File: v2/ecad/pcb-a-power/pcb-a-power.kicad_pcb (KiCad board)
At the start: 4 copper layers, 285 x 160 mm, 214 parts, among them Q5 2N7002: Pi GPIO high = pull K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, U19 PCA9555PW (0x21), U20 BQ25792 1S charger from SHORE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, U21 BQ34Z100-G1 gauge (I2C 0x55, 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, U22 TPS61288L boost +5V_M1 (15 A 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, U23 TPS61288L boost +5V_M2 (15 A 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, U24 TPS61288L boost +5V_PI (15 A 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, U25 LTC2954CTS8-1 push-button on/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, U26 TPS259571DSGR eFuse 12 V 2.0 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, U28 TPS2065CDBV, U29 INA219AIDCN, U30 USBLC6-2SC6, U31 PCA9555PW (0x24): wall port, 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, U5 TPS563201 3.3 V buck from M1

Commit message: fix(release): A20 and E4 relabelled GNSS post-route, E5 block with one outline around the power targets; deliverables, order and review sets rebuilt [MESHSAT-795]
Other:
- board text added: "BM GNSS"
- board text added: "SMA GNSS"
- board text removed: "BM WIFI 5.8"
- board text removed: "SMA WIFI 5.8"
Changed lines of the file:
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@@
 		)
 	)
-	(gr_text "SMA WIFI 5.8"
+	(gr_text "SMA GNSS"
 		(at 124 160 0)
 		(layer "F.SilkS")
@@
 		)
 	)
-	(gr_text "BM WIFI 5.8"
+	(gr_text "BM GNSS"
 		(at 124 184 0)
 		(layer "B.SilkS")

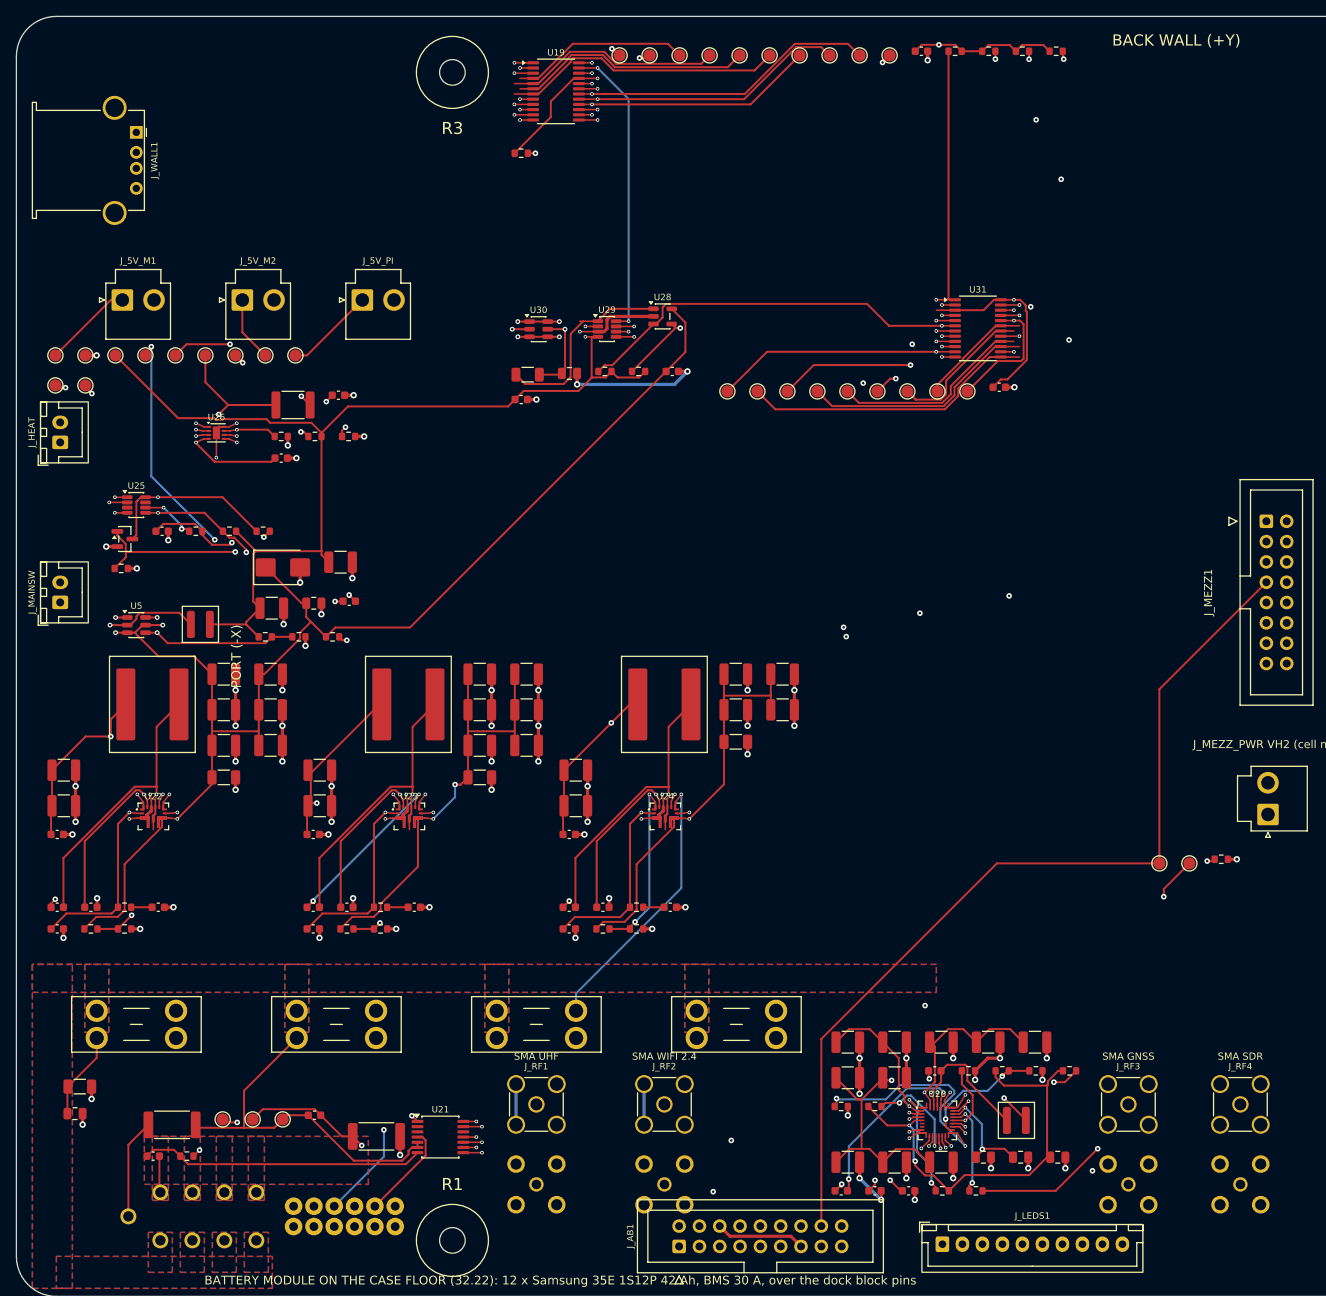
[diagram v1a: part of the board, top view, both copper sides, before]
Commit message: feat(pcb-a): A21, PCB-A re-routed with the net classes applied: rail islands and bottom bands, boost feeds on In2 and B.Cu, 0.6 mm cell-node links, USB pairs 0.2/0.15 [MESHSAT-795]
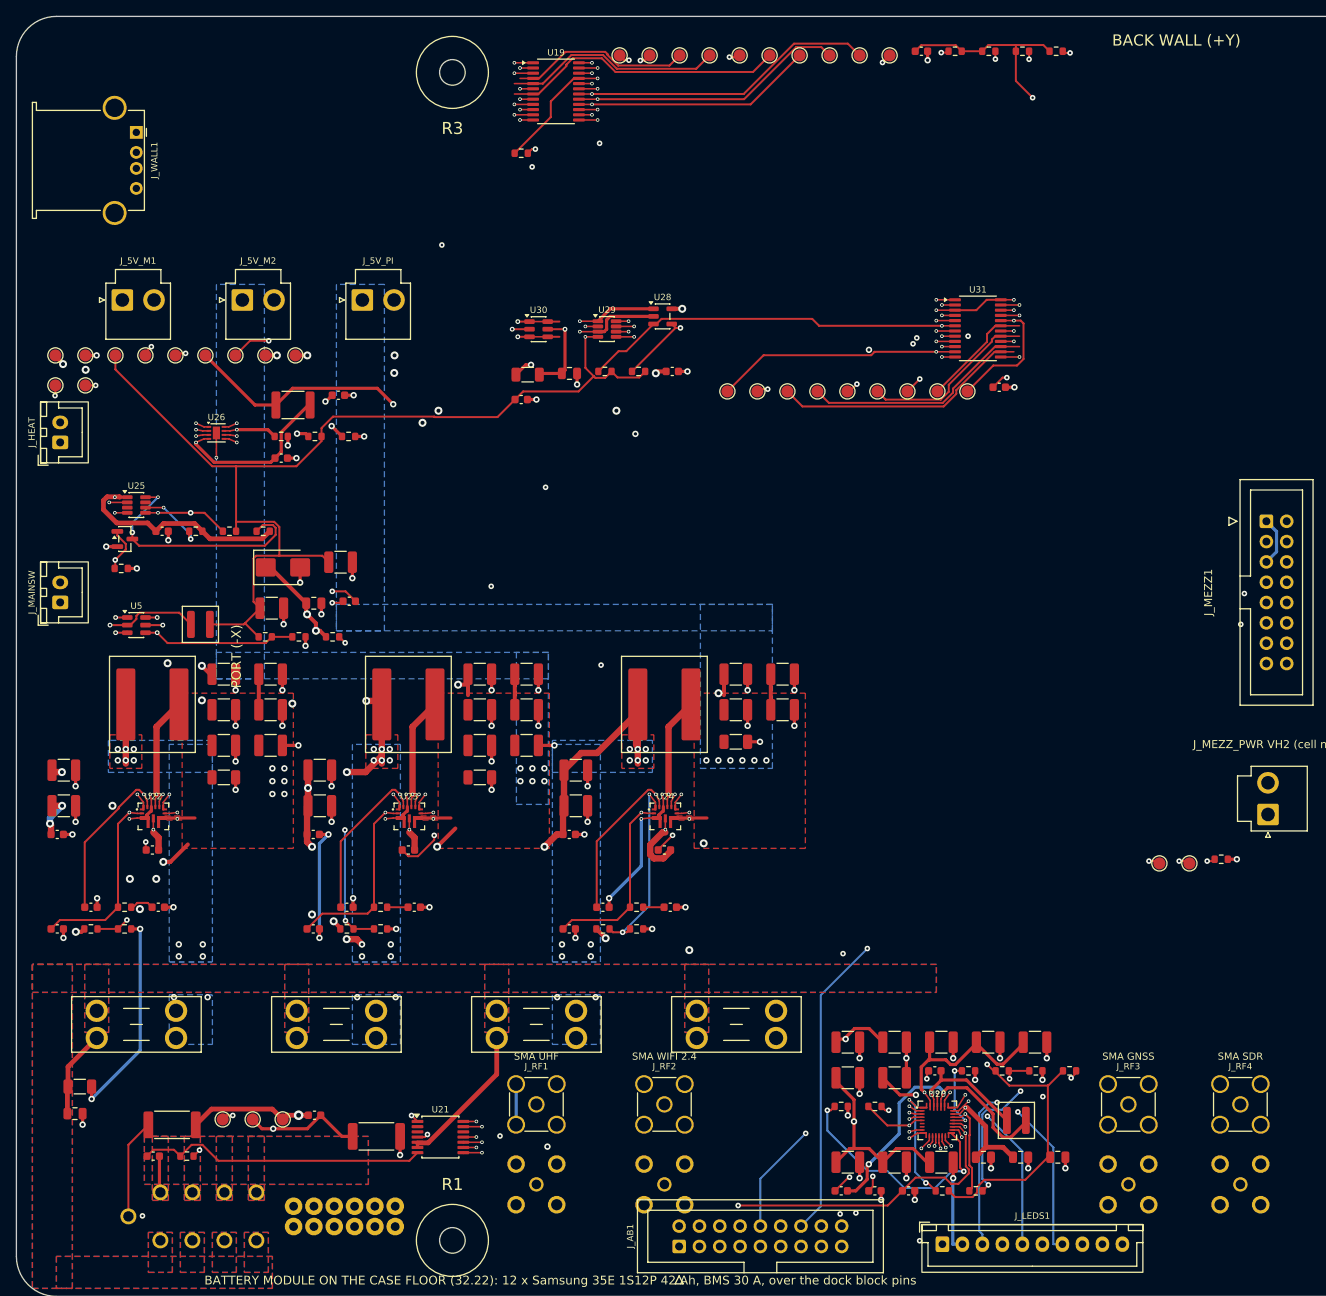
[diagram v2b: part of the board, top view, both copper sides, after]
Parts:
- moved C84 13.9 mm to (66.0, 134.2)
- moved C38 13.9 mm to (2.00, 134.2)
- moved C71 13.9 mm to (34.0, 134.2)
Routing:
- net GND: track 1441.6 -> 1514.2 mm
- net /+5V_M2: track 136.1 -> 103.6 mm, vias 2 -> 12
- net /SHORE_12V: track 241.7 -> 272.8 mm, vias 5 -> 8
- net /SCL: track 338.2 -> 308.0 mm, vias 7 -> 6
- net /BOOST1_IN: track 65.1 -> 84.0 mm, vias 2 -> 19
- net /I2S_BCLK: track 131.5 -> 150.2 mm, vias 1 -> 0
- net /LED_MESH_K: track 198.1 -> 180.6 mm
- net /BST3: track 26.9 -> 9.50 mm
- net /LED_LTE_K: track 198.9 -> 181.9 mm, vias 2 -> 1
- net /DOCK_SPARE: track 130.7 -> 147.7 mm, vias 1 -> 2
- net /LED_SYS_K: track 208.3 -> 191.5 mm, vias 2 -> 1
- net /+5V_PI: track 149.7 -> 133.0 mm, vias 1 -> 15
- net /PI_KILL: track 131.4 -> 147.1 mm, vias 1 -> 2
- net /SW1: track 38.4 -> 22.8 mm, vias 1 -> 2
- net /SW2: track 38.4 -> 22.8 mm, vias 1 -> 2
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- added copper zone on F.Cu, net /+5V_M1
- added copper zone on B.Cu, net /+5V_M2
- added copper zone on F.Cu, net /+5V_M2
- added copper zone on B.Cu, net /+5V_PI
- added copper zone on F.Cu, net /+5V_PI
- added copper zone on B.Cu, net /BOOST1_IN
- added copper zone on F.Cu, net /BOOST1_IN
- added copper zone on In1.Cu, net /BOOST1_IN
- added copper zone on In2.Cu, net /BOOST1_IN
- added copper zone on B.Cu, net /BOOST2_IN
- added copper zone on F.Cu, net /BOOST2_IN
- added copper zone on In1.Cu, net /BOOST2_IN
- added copper zone on In2.Cu, net /BOOST2_IN
- added copper zone on B.Cu, net /BOOST3_IN
- added copper zone on F.Cu, net /BOOST3_IN
- added copper zone on In1.Cu, net /BOOST3_IN
- added copper zone on In2.Cu, net /BOOST3_IN

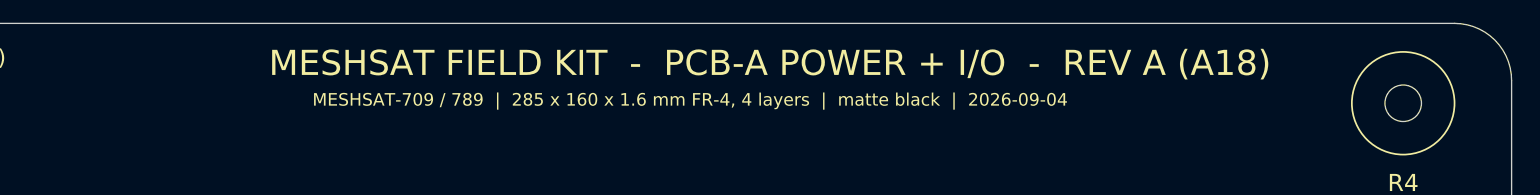
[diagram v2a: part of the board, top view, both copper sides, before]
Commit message: fix(pcb): A21 and D7 boards retitled to their phase and date, deliverables re-exported [MESHSAT-795]
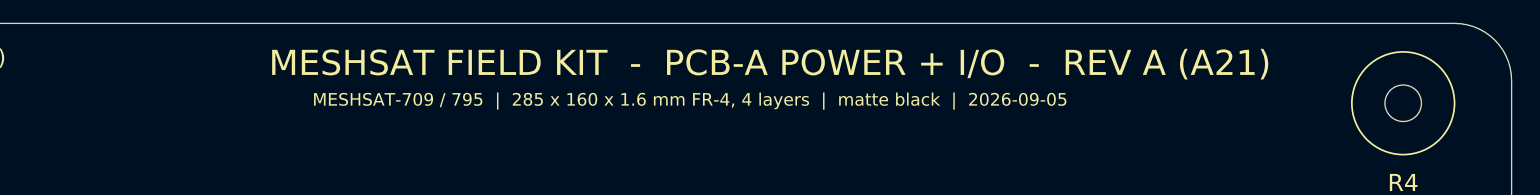
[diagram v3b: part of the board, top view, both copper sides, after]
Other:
- board text added: "MESHSAT FIELD KIT - PCB-A POWER + I/O - REV A (A21)"
- board text added: "MESHSAT-709 / 795 | 285 x 160 x 1.6 mm FR-4, 4 layers | matte black | 2026-09-05"
- board text removed: "MESHSAT FIELD KIT - PCB-A POWER + I/O - REV A (A18)"
- board text removed: "MESHSAT-709 / 789 | 285 x 160 x 1.6 mm FR-4, 4 layers | matte black | 2026-09-04"
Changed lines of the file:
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@@
 	(title_block
 		(title "MeshSat Field Kit carrier - PCB-B COMPUTE")
-		(date "2026-09-02")
-		(rev "A")
+		(date "2026-09-05")
+		(rev "A (A21)")
 		(company "MeshSat")
 		(comment 1 "MESHSAT-709. Case-centred frame. Phase B1 mechanical + placement. tools/gen_pcb_b.py")
@@
 		)
 	)
-	(gr_text "MESHSAT-709 / 789  |  285 x 160 x 1.6 mm FR-4, 4 layers  |  matte black  |  2026-09-04"
+	(gr_text "MESHSAT-709 / 795  |  285 x 160 x 1.6 mm FR-4, 4 layers  |  matte black  |  2026-09-05"
 		(at 198 36.7 0)
 		(layer "F.SilkS")
@@
 		)
 	)
-	(gr_text "MESHSAT FIELD KIT  -  PCB-A POWER + I/O  -  REV A (A18)"
+	(gr_text "MESHSAT FIELD KIT  -  PCB-A POWER + I/O  -  REV A (A21)"
 		(at 205 33.5 0)
 		(layer "F.SilkS")

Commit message: feat(release): A22 (six layers, run 12 with the hand closures) routed clean on the box, deliverable meshsat-pcb-a-revA-A22 [MESHSAT-830]
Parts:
- removed C105: 100n, C_0603_1608Metric
- removed F2: 10 A mini blade (Keystone 3568 holder): pack node to the 8 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, Fuseholder_Blade_Mini_Keystone_3568
- removed F3: 10 A mini blade (Keystone 3568 holder): pack node to the M1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, Fuseholder_Blade_Mini_Keystone_3568
- removed F4: 10 A mini blade (Keystone 3568 holder): pack node to the M2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, Fuseholder_Blade_Mini_Keystone_3568
- removed F5: 15 A mini blade (Keystone 3568 holder): pack node to the Pi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, Fuseholder_Blade_Mini_Keystone_3568
- removed F6: 2.5A hold 30V 1812, Fuse_1812_4532Metric
- removed J_5V_M1: rail M1 to PCB-B J_5V_M1 (JST-VH, 18 AWG): + -, JST_VH_B2P-VH_1x02_P3.96mm_Vertical
- removed J_5V_M2: rail M2 to PCB-B J_5V_M2 (JST-VH, 18 AWG): + -, JST_VH_B2P-VH_1x02_P3.96mm_Vertical
- removed J_5V_PI: Pi rail 5.1 V 5 A to PCB-B J_5V_PI (JST-VH, 18 AWG): + -, JST_VH_B2P-VH_1x02_P3.96mm_Vertical
- removed J_LEDS1: front-wall LED row (XH2.5): PWR MESH SAT LTE SYS, JST_XH_B10B-XH-A_1x10_P2.50mm_Vertical
- removed J_WALL1: USB-A receptacle, internal cable to the Glenair 233-370 wal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, USB_A_Stewart_SS-52100-001_Horizontal
- removed RT1: 10k NTC 0603 1% (gauge temperature, beside the dock pins; t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, R_0603_1608Metric
- removed TP1: +5V_M1, TestPoint_Pad_D1.5mm
- removed TP2: GND, TestPoint_Pad_D1.5mm
- removed TP27: EXP2_SP8, TestPoint_Pad_D1.5mm
- removed TP29: EXP_SP4, TestPoint_Pad_D1.5mm
- removed TP30: EXP_SP5, TestPoint_Pad_D1.5mm
- removed TP31: EXP_SP6, TestPoint_Pad_D1.5mm
- removed TP32: EXP_SP7, TestPoint_Pad_D1.5mm
- removed TP33: EXP_SP8, TestPoint_Pad_D1.5mm
- removed TP34: EXP_SP9, TestPoint_Pad_D1.5mm
- removed TP35: EXP_SP10, TestPoint_Pad_D1.5mm
- removed TP36: EXP_SP11, TestPoint_Pad_D1.5mm
- removed U20: BQ25792 1S charger from SHORE_12V (3 A set over ILIM_HIZ, 7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, Texas_RQM0029A_QFN-29_4x4mm
- removed U24: TPS61288L boost +5V_PI (15 A switch, 500 kHz, no MODE pin), Texas_RQQ0011A_VQFN-HR-11_2.5x3mm
- removed U25: LTC2954CTS8-1 push-button on/off controller, TSOT-23-8
- removed U30: USBLC6-2SC6, SOT-23-6
- removed U31: PCA9555PW (0x24): wall port, heating pad, charger, gauge, TSSOP-24_4.4x7.8mm_P0.65mm
- added C1: 100u 25V, C_1206_3216Metric, F.Cu at (40.8, 166.6)
- added C10: 100n 25V, C_0603_1608Metric, F.Cu at (38.3, 75.6)
- added C102: 10n, C_0603_1608Metric, F.Cu at (236.1, 60.2)
- added C103: 100n, C_0603_1608Metric, F.Cu at (244.5, 62.9)
- added C109: 22u 50V X7R 1210, C_1210_3225Metric, F.Cu at (136.9, 139.7)
- added C11: 22u 50V X7R 1210, C_1210_3225Metric, F.Cu at (78.9, 66.2)
- added C110: 22u 50V X7R 1210, C_1210_3225Metric, F.Cu at (142.8, 139.7)
- added C111: 22u 50V X7R 1210, C_1210_3225Metric, F.Cu at (136.9, 144.1)
- added C112: 3.3n, C_0603_1608Metric, F.Cu at (90.3, 73.0)
- added C113: 3.3n, C_0603_1608Metric, F.Cu at (106.3, 73.0)
- added C114: 3.3n, C_0603_1608Metric, F.Cu at (122.3, 73.0)
- added C115: 3.3n, C_0603_1608Metric, F.Cu at (142.5, 73.0)
- added C116: 22u 50V X7R 1210, C_1210_3225Metric, F.Cu at (188.8, 61.0)
- added C117: 22u 50V X7R 1210, C_1210_3225Metric, F.Cu at (194.6, 61.0)
- added C118: 22u 50V X7R 1210, C_1210_3225Metric, F.Cu at (200.5, 61.0)
- added C119: 22u 50V X7R 1210, C_1210_3225Metric, F.Cu at (206.3, 61.0)
- added C12: 22u 50V X7R 1210, C_1210_3225Metric, F.Cu at (34.9, 72.0)
- added C120: 10u 25V 1210, C_1210_3225Metric, F.Cu at (161.8, 57.0)
- added C16: 100n 25V, C_0603_1608Metric, F.Cu at (58.1, 105.4)
- added C17: 100n 25V, C_0603_1608Metric, F.Cu at (62.3, 105.4)
- added C18: 3.3u, C_0805_2012Metric, F.Cu at (42.4, 105.6)
- added C19: 1u, C_0603_1608Metric, F.Cu at (70.7, 105.4)
- added C2: 100u 25V, C_1206_3216Metric, F.Cu at (34.9, 171.1)
- added C20: 10u 35V 1210, C_1210_3225Metric, F.Cu at (43.8, 86.0)
- added C21: 10u 35V 1210, C_1210_3225Metric, F.Cu at (49.7, 86.0)
- added C22: 10u 35V 1210, C_1210_3225Metric, F.Cu at (55.5, 86.0)
- added C23: 22u 25V 1210, C_1210_3225Metric, F.Cu at (61.4, 86.0)
- added C24: 22u 25V 1210, C_1210_3225Metric, F.Cu at (67.2, 86.0)
- added C25: 22u 25V 1210, C_1210_3225Metric, F.Cu at (73.1, 86.0)
- added C26: 10n, C_0603_1608Metric, F.Cu at (62.4, 110.0)
- added C27: 1n, C_0603_1608Metric, F.Cu at (66.6, 110.0)
- added C28: 100n, C_0603_1608Metric, F.Cu at (92.0, 65.8)
- added C29: 10u 25V 1210, C_1210_3225Metric, F.Cu at (86.9, 49.2)
- added C3: 10u 25V 1210, C_1210_3225Metric, F.Cu at (34.9, 167.1)
- added C30: 10u 25V 1210, C_1210_3225Metric, F.Cu at (92.8, 49.2)
- added C31: 22u 10V X7R 1210, C_1210_3225Metric, F.Cu at (86.9, 62.2)
- added C32: 22u 10V X7R 1210, C_1210_3225Metric, F.Cu at (92.8, 62.2)
- added C33: 22u 10V X7R 1210, C_1210_3225Metric, F.Cu at (86.9, 66.7)
- added C34: 100n, C_0603_1608Metric, F.Cu at (108.0, 65.8)
- added C35: 10u 25V 1210, C_1210_3225Metric, F.Cu at (102.9, 49.2)
- added C36: 10u 25V 1210, C_1210_3225Metric, F.Cu at (108.8, 49.2)
- added C37: 22u 10V X7R 1210, C_1210_3225Metric, F.Cu at (102.9, 62.2)
- added C4: 1u, C_0603_1608Metric, F.Cu at (209.2, 135.4)
- added C5: 10n, C_0603_1608Metric, F.Cu at (73.2, 71.1)
- added C6: 100p, C_0603_1608Metric, F.Cu at (77.4, 71.1)
- added C8: 4.7u, C_0805_2012Metric, F.Cu at (40.2, 71.4)
- added C9: 100n 25V, C_0603_1608Metric, F.Cu at (34.1, 75.6)
- added D1: SMCJ18A (VBAT clamp), D_SMB, F.Cu at (36.3, 156.9)
- added D3: SMBJ5.0A, D_SMB, F.Cu at (123.3, 114.9)
- added D4: SMBJ18A (VBUS clamp at the outlet), D_SMB, F.Cu at (163.1, 50.9)
- added F1: 25 A mini blade (Keystone 3568 holder): pack node to VBAT, Fuseholder_Blade_Mini_Keystone_3568, F.Cu at (48.0, 160.3)
- added J_54V: 54 V to the PoE injector on B16 (JST-VH): + -, JST_VH_B2P-VH_1x02_P3.96mm_Vertical, F.Cu at (259.4, 111.8)
- added J_5V_DEV: USB device rail to B16 (JST-VH): + -, JST_VH_B2P-VH_1x02_P3.96mm_Vertical, F.Cu at (128.2, 34.5)
- added J_5V_S1: slot 1 5.1 V rail to B16 (JST-VH, 16 AWG): + -, JST_VH_B2P-VH_1x02_P3.96mm_Vertical, F.Cu at (92.2, 34.5)
- added J_5V_S2: slot 2 5.1 V rail to B16 (JST-VH, 16 AWG): + -, JST_VH_B2P-VH_1x02_P3.96mm_Vertical, F.Cu at (104.2, 34.5)
- added J_5V_S3: slot 3 5.1 V rail to B16 (JST-VH, 16 AWG): + -, JST_VH_B2P-VH_1x02_P3.96mm_Vertical, F.Cu at (116.2, 34.5)
- added J_BM10: SMP-MAX slide-on receptacle R222M00720 (underside), IRID to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, Radiall_SMPMAX_R222M00720, B.Cu at (238.0, 176.0)
- added J_BM11: SMP-MAX slide-on receptacle R222M00720 (underside), LORA to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, Radiall_SMPMAX_R222M00720, B.Cu at (250.0, 176.0)
- added J_BM8: SMP-MAX slide-on receptacle R222M00720 (underside), 5G-MAIN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, Radiall_SMPMAX_R222M00720, B.Cu at (210.0, 176.0)
- added J_BM9: SMP-MAX slide-on receptacle R222M00720 (underside), 5G-DIV 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, Radiall_SMPMAX_R222M00720, B.Cu at (224.0, 176.0)
- added J_HF: 12.0 V to the QMX HF unit in its lid tray (JST-VH, in the l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, JST_VH_B2P-VH_1x02_P3.96mm_Vertical, F.Cu at (259.4, 99.8)
- added J_MON: monitor supply lead to the Xenarc (JST-VH): + -, JST_VH_B2P-VH_1x02_P3.96mm_Vertical, F.Cu at (259.4, 61.8)
- added J_PA: 13.8 V to the PA module on the face plate (JST-VH, 16 AWG):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, JST_VH_B2P-VH_1x02_P3.96mm_Vertical, F.Cu at (259.4, 49.8)
- added J_RF10: SMA jack (Amphenol 132134, vertical), pigtail from the IRID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, SMA_Amphenol_132134-11_Vertical, F.Cu at (238.0, 166.0)
- added J_RF11: SMA jack (Amphenol 132134, vertical), pigtail from the LORA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, SMA_Amphenol_132134-11_Vertical, F.Cu at (250.0, 166.0)
- added J_RF8: SMA jack (Amphenol 132134, vertical), pigtail from the 5G-M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, SMA_Amphenol_132134-11_Vertical, F.Cu at (210.0, 166.0)
- added J_RF9: SMA jack (Amphenol 132134, vertical), pigtail from the 5G-D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, SMA_Amphenol_132134-11_Vertical, F.Cu at (224.0, 166.0)
- added J_USBC_OUT: wall USB-C outlet, power side (pigtail header): VBUS CC1 CC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, PinHeader_1x05_P2.54mm_Vertical, F.Cu at (254.9, 84.0)
- added J_USBW: wall USB-C data pair to B16 passes here on the ribbon: this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, JST_PH_B4B-PH-K_1x04_P2.00mm_Vertical, F.Cu at (259.4, 125.0)
- added L1: 10uH XAL1010-103ME (Isat 14 A), L_Coilcraft_XAL1010-XXX, F.Cu at (72.0, 52.0)
- added L10: 22uH XAL1010-223ME (Isat 9 A), L_Coilcraft_XAL1010-XXX, F.Cu at (72.0, 134.0)
- added L11: 6.8uH XAL1010-682ME, L_Coilcraft_XAL1010-XXX, F.Cu at (206.0, 45.0)
- added L7: 4.7uH XAL4030-472ME, L_Coilcraft_XAL4030-XXX, F.Cu at (92.0, 99.5)
- added L8: 6.8uH XAL1010-682ME (Isat 17 A), L_Coilcraft_XAL1010-XXX, F.Cu at (124.0, 106.0)
- added L9: 6.8uH XAL1010-682ME, L_Coilcraft_XAL1010-XXX, F.Cu at (128.0, 137.0)
- added Q1: 2N7002: panel controller high = pull KILL low = power off (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, SOT-23, F.Cu at (204.6, 136.3)
- added Q10: CSD18510Q5B 40 V N-FET, PowerPAK_SO-8_Single, F.Cu at (62.8, 80.4)
- added Q11: CSD18510Q5B 40 V N-FET, PowerPAK_SO-8_Single, F.Cu at (88.6, 115.4)
- added Q12: CSD18510Q5B 40 V N-FET, PowerPAK_SO-8_Single, F.Cu at (97.3, 115.4)
- added Q13: CSD18510Q5B 40 V N-FET, PowerPAK_SO-8_Single, F.Cu at (106.0, 115.4)
- added Q14: CSD18510Q5B 40 V N-FET, PowerPAK_SO-8_Single, F.Cu at (114.8, 115.4)
- added Q15: CSD18510Q5B 40 V N-FET, PowerPAK_SO-8_Single, F.Cu at (108.6, 147.4)
- added Q16: CSD18510Q5B 40 V N-FET, PowerPAK_SO-8_Single, F.Cu at (117.3, 147.4)
- added Q17: 100 V N-FET PowerPAK SO-8 (CSD19536KTT class), PowerPAK_SO-8_Single, F.Cu at (36.6, 145.4)
- added Q18: 100 V N-FET PowerPAK SO-8 (CSD19536KTT class), PowerPAK_SO-8_Single, F.Cu at (45.3, 145.4)
- added Q19: 100 V N-FET PowerPAK SO-8 (CSD19536KTT class), PowerPAK_SO-8_Single, F.Cu at (54.0, 145.4)
- added Q2: 60 V N-FET PowerPAK SO-8 (CSD19532Q5B class), PowerPAK_SO-8_Single, F.Cu at (36.6, 43.4)
- added Q20: 100 V N-FET PowerPAK SO-8 (CSD19536KTT class), PowerPAK_SO-8_Single, F.Cu at (62.8, 145.4)
- added Q21: CSD18510Q5B 40 V N-FET, PowerPAK_SO-8_Single, F.Cu at (184.6, 55.4)
- added Q22: CSD18510Q5B 40 V N-FET, PowerPAK_SO-8_Single, F.Cu at (193.3, 55.4)
- added Q23: CSD18510Q5B 40 V N-FET, PowerPAK_SO-8_Single, F.Cu at (126.0, 147.4)
- added Q24: CSD18510Q5B 40 V N-FET, PowerPAK_SO-8_Single, F.Cu at (108.6, 154.1)
- added Q25: CSD18510Q5B 40 V N-FET, PowerPAK_SO-8_Single, F.Cu at (202.0, 55.4)
- added Q26: CSD18510Q5B 40 V N-FET, PowerPAK_SO-8_Single, F.Cu at (210.8, 55.4)
- added Q27: CSD18510Q5B 40 V N-FET (VBUS switch), PowerPAK_SO-8_Single, F.Cu at (154.6, 51.4)
- added Q3: 60 V N-FET PowerPAK SO-8 (CSD19532Q5B class), PowerPAK_SO-8_Single, F.Cu at (45.3, 43.4)
- added Q4: 60 V N-FET PowerPAK SO-8 (CSD19532Q5B class), PowerPAK_SO-8_Single, F.Cu at (36.6, 50.1)
- added Q6: 2N7002: CHG_INHIBIT high = ILIM_HIZ low = charger in HiZ, SOT-23, F.Cu at (37.6, 106.3)
- added Q7: CSD18510Q5B 40 V N-FET, PowerPAK_SO-8_Single, F.Cu at (36.6, 80.4)
- added Q8: CSD18510Q5B 40 V N-FET, PowerPAK_SO-8_Single, F.Cu at (45.3, 80.4)
- added Q9: CSD18510Q5B 40 V N-FET, PowerPAK_SO-8_Single, F.Cu at (54.0, 80.4)
- added R1: 10R 2W 2512, R_2512_6332Metric, F.Cu at (36.5, 162.3)
- added R10: 10k, R_0603_1608Metric, F.Cu at (68.9, 71.1)
- added R100: 100k 1%, R_0603_1608Metric, F.Cu at (236.1, 62.9)
- added R101: 10k 1% (OVLO), R_0603_1608Metric, F.Cu at (240.3, 62.9)
- added R102: 10k, R_0603_1608Metric, F.Cu at (230.3, 135.4)
- added R103: 100k, R_0603_1608Metric, F.Cu at (204.1, 140.0)
- added R104: 100k, R_0603_1608Metric, F.Cu at (208.3, 140.0)
- added R11: 10mOhm 1% 2512 (ISNS), R_2512_6332Metric, F.Cu at (45.0, 66.6)
- added R110: 10k, R_0603_1608Metric, F.Cu at (220.9, 140.0)
- added R111: 100k, R_0603_1608Metric, F.Cu at (225.2, 140.0)
- added R112: 100k, R_0603_1608Metric, F.Cu at (229.4, 140.0)
- added R113: 100k, R_0603_1608Metric, F.Cu at (233.6, 140.0)
- added R114: 100k, R_0603_1608Metric, F.Cu at (237.8, 140.0)
- added R115: 68k (RT: 500 kHz), R_0603_1608Metric, F.Cu at (134.1, 73.0)
- added R116: 100k, R_0603_1608Metric, F.Cu at (195.9, 142.4)
- added R117: 10k, R_0603_1608Metric, F.Cu at (162.1, 146.1)
- added R118: 100k, R_0603_1608Metric, F.Cu at (166.3, 146.1)
- added R119: 100k (MODE: CCM), R_0603_1608Metric, F.Cu at (55.2, 75.6)
- added R12: 5mOhm 1% 2512 (CS), R_2512_6332Metric, F.Cu at (54.0, 66.6)
- added R120: 100k (MODE: CCM), R_0603_1608Metric, F.Cu at (98.7, 94.6)
- added R121: 100k (MODE: CCM), R_0603_1608Metric, F.Cu at (62.4, 125.3)
- added R122: 5mOhm 1% 2512 (CS), R_2512_6332Metric, F.Cu at (126.1, 153.3)
- added R123: 100k, R_0603_1608Metric, F.Cu at (140.3, 155.8)
- added R124: 62k 1%, R_0603_1608Metric, F.Cu at (144.5, 155.8)
- added R125: 10k 1%, R_0603_1608Metric, F.Cu at (136.1, 158.5)
- added R126: 100k (MODE: CCM), R_0603_1608Metric, F.Cu at (140.3, 158.5)
- added R127: 5mOhm 1% 2512 (CS), R_2512_6332Metric, F.Cu at (228.3, 54.6)
- added R128: 100k, R_0603_1608Metric, F.Cu at (207.4, 64.6)
- added R129: 22k, R_0603_1608Metric, F.Cu at (86.1, 73.0)
- added R13: 100k, R_0603_1608Metric, F.Cu at (42.5, 75.6)
- added R130: 22k, R_0603_1608Metric, F.Cu at (102.1, 73.0)
- added R131: 22k, R_0603_1608Metric, F.Cu at (118.1, 73.0)
- added R132: 22k, R_0603_1608Metric, F.Cu at (138.3, 73.0)
- added R133: 62k 1%, R_0603_1608Metric, F.Cu at (211.6, 64.6)
- added R134: 10k 1%, R_0603_1608Metric, F.Cu at (215.8, 64.6)
- added R135: 100k (MODE: CCM), R_0603_1608Metric, F.Cu at (220.0, 64.6)
- added R136: 21.0k 1% (R_FBL2: 9 V when CTL2 is low), R_0603_1608Metric, F.Cu at (160.5, 61.2)
- added R137: 14.0k 1% (R_FBL1: 15 V when CTL1 is low too), R_0603_1608Metric, F.Cu at (164.7, 61.2)
- added R138: 10mOhm 1% 2512 (ISNS), R_2512_6332Metric, F.Cu at (171.8, 50.6)
- added R139: 43R 1W 2512 (DSCG), R_2512_6332Metric, F.Cu at (154.5, 57.3)
- added R14: 62k 1%, R_0603_1608Metric, F.Cu at (46.7, 75.6)
- added R140: 1M (GD to VPWR, 9.1.3), R_0603_1608Metric, F.Cu at (168.9, 61.2)
- added R141: 700k, R_0603_1608Metric, F.Cu at (173.2, 61.2)
- added R142: 10k, R_0603_1608Metric, F.Cu at (177.4, 61.2)
- added R143: 100k, R_0603_1608Metric, F.Cu at (152.1, 63.9)
- added R15: 10k 1%, R_0603_1608Metric, F.Cu at (50.9, 75.6)
- added R16: 10mOhm 1% 2512 (RAC, input current sense), R_2512_6332Metric, F.Cu at (71.4, 79.6)
- added R17: 5mOhm 1% 2512 (RSR, charge current sense), R_2512_6332Metric, F.Cu at (36.5, 86.3)
- added R19: 16.5k 1%, R_0603_1608Metric, F.Cu at (75.0, 105.4)
- added R2: 100k, R_0603_1608Metric, F.Cu at (213.4, 135.4)
- added R20: 34.8k 1%, R_0603_1608Metric, F.Cu at (37.1, 110.0)
- added R21: 100k, R_0603_1608Metric, F.Cu at (41.3, 110.0)
- added R22: 10k, R_0603_1608Metric, F.Cu at (45.5, 110.0)
- added R23: 10k, R_0603_1608Metric, F.Cu at (49.7, 110.0)
- added R24: 10k (PSYS load), R_0603_1608Metric, F.Cu at (53.9, 110.0)
- added R25: 10k, R_0603_1608Metric, F.Cu at (58.2, 110.0)
- added R26: 60.4k 1% (CELL_BATPRESZ: 4S per Table, from VDDA), R_0603_1608Metric, F.Cu at (70.8, 110.0)
- added R27: 40.2k 1%, R_0603_1608Metric, F.Cu at (75.0, 110.0)
- added R28: 53.6k 1%, R_0603_1608Metric, F.Cu at (96.2, 65.8)
- added R29: 10k 1%, R_0603_1608Metric, F.Cu at (86.1, 70.3)
- added R3: 100k, R_0603_1608Metric, F.Cu at (217.6, 135.4)
- added R30: 100k, R_0603_1608Metric, F.Cu at (90.3, 70.3)
- added R31: 5mOhm 1% 2512 (shunt), R_2512_6332Metric, F.Cu at (88.5, 87.1)
- added R32: 53.6k 1%, R_0603_1608Metric, F.Cu at (112.2, 65.8)
- added R33: 10k 1%, R_0603_1608Metric, F.Cu at (102.1, 70.3)
- added R4: 100k, R_0603_1608Metric, F.Cu at (221.8, 135.4)
- added R40: 53.6k 1%, R_0603_1608Metric, F.Cu at (144.2, 65.8)
- added R41: 10k 1%, R_0603_1608Metric, F.Cu at (134.1, 70.3)
- added R42: 100k, R_0603_1608Metric, F.Cu at (138.3, 70.3)
- added R43: 5mOhm 1% 2512 (shunt), R_2512_6332Metric, F.Cu at (115.2, 87.1)
- added R45: 68k (RT: 500 kHz), R_0603_1608Metric, F.Cu at (94.5, 70.3)
- added R46: 68k (RT: 500 kHz), R_0603_1608Metric, F.Cu at (110.5, 70.3)
- added R49: 10k 1%, R_0603_1608Metric, F.Cu at (94.5, 107.8)
- added R5: 100k, R_0603_1608Metric, F.Cu at (226.1, 135.4)
- added R50: 162k 1%, R_0603_1608Metric, F.Cu at (90.8, 91.4)
- added R6: 240k 1%, R_0603_1608Metric, F.Cu at (52.1, 71.1)
- added R7: 10k 1%, R_0603_1608Metric, F.Cu at (56.3, 71.1)
- added R79: 30k (slope), R_0603_1608Metric, F.Cu at (228.6, 60.1)
- added R8: 40.2k (300 kHz), R_0603_1608Metric, F.Cu at (60.5, 71.1)
- added R80: 10k, R_0603_1608Metric, F.Cu at (182.1, 64.6)
- added R81: 10mOhm 1% 2512 (ISNS), R_2512_6332Metric, F.Cu at (219.4, 54.6)
- added R9: 30k (slope), R_0603_1608Metric, F.Cu at (64.7, 71.1)
- added R90: 1.2 A (ILM), R_0603_1608Metric, F.Cu at (240.3, 49.4)
- added R91: 10k, R_0603_1608Metric, F.Cu at (244.5, 49.4)
- added R92: 100k 1%, R_0603_1608Metric, F.Cu at (236.1, 52.1)
- added R93: 10k 1% (OVLO), R_0603_1608Metric, F.Cu at (240.3, 52.1)
- added R94: 1.0 A (ILM), R_0603_1608Metric, F.Cu at (240.3, 54.8)
- added R95: 10k, R_0603_1608Metric, F.Cu at (244.5, 54.8)
- added R96: 100k 1%, R_0603_1608Metric, F.Cu at (236.1, 57.5)
- added R97: 10k 1% (OVLO), R_0603_1608Metric, F.Cu at (240.3, 57.5)
- added R98: 2.0 A (ILM), R_0603_1608Metric, F.Cu at (240.3, 60.2)
- added R99: 10k, R_0603_1608Metric, F.Cu at (244.5, 60.2)
- added U1: LTC2954CTS8-1 push-button on/off controller, TSOT-23-8, F.Cu at (101.0, 138.1)
- added U10: INA226 rail monitor +5V_S3, VSSOP-10_3x3mm_P0.5mm, F.Cu at (111.0, 82.0)
- added U11: INA226 rail monitor +5V_DEV, VSSOP-10_3x3mm_P0.5mm, F.Cu at (123.0, 82.0)
- added U12: TPS62933DRLR 3 A buck, 3.3 V logic, SOT-583-8, F.Cu at (86.0, 99.6)
- added U13: LM5176PWPR buck-boost controller, +13V8_PA from VBAT, HTSSOP-28-1EP_4.4x9.7mm_P0.65mm_EP2.85x5.4mm, F.Cu at (106.0, 104.0)
- added U14: INA226 PA rail monitor (0x46), VSSOP-10_3x3mm_P0.5mm, F.Cu at (135.0, 82.0)
- added U15: LM5176PWPR buck-boost controller, +12V_HF from VBAT, HTSSOP-28-1EP_4.4x9.7mm_P0.65mm_EP2.85x5.4mm, F.Cu at (114.0, 137.0)
- added U16: LM5176PWPR buck-boost controller, +54V_POE from VBAT, HTSSOP-28-1EP_4.4x9.7mm_P0.65mm_EP2.85x5.4mm, F.Cu at (54.0, 136.0)
- added U17: INA226 PoE rail monitor (0x47), VSSOP-10_3x3mm_P0.5mm, F.Cu at (40.4, 120.0)
- added U18: TPS25740ARGER USB-C PD source controller, 45 W outlet (5, 9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, QFN-24-1EP_4x4mm_P0.5mm_EP2.5x2.5mm, F.Cu at (160.2, 45.0)
- added U2: LM5176PWPR buck-boost controller, VBUS20 from VIN_RAW, HTSSOP-28-1EP_4.4x9.7mm_P0.65mm_EP2.85x5.4mm, F.Cu at (56.0, 54.0)
- added U27: PCA9555PW (0x21): enables and status, TSSOP-24_4.4x7.8mm_P0.65mm, F.Cu at (100.2, 129.0)
- added U3: BQ25731RSNR 1 to 5 cell buck-boost charger, 4S from the 20 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, QFN-32-1EP_4x4mm_P0.4mm_EP2.65x2.65mm, F.Cu at (54.2, 98.0)
- added U4: AP64500SP-13 5 A buck, 5.1 V rail +5V_S1, SOIC-8-1EP_3.9x4.9mm_P1.27mm_EP2.29x3mm, F.Cu at (90.0, 44.1)
- added U6: AP64500SP-13 5 A buck, 5.1 V rail +5V_S3, SOIC-8-1EP_3.9x4.9mm_P1.27mm_EP2.29x3mm, F.Cu at (122.0, 44.1)
- added U7: AP64500SP-13 5 A buck, 5.1 V rail +5V_DEV, SOIC-8-1EP_3.9x4.9mm_P1.27mm_EP2.29x3mm, F.Cu at (138.0, 44.1)
- added U8: INA226 rail monitor +5V_S1, VSSOP-10_3x3mm_P0.5mm, F.Cu at (87.0, 82.0)
- added U9: INA226 rail monitor +5V_S2, VSSOP-10_3x3mm_P0.5mm, F.Cu at (99.0, 82.0)
- C100, C68: value 100n -> 10n
- C101, C46, C93: value 22u 10V X7R 1210 -> 100n; footprint C_1210_3225Metric -> C_0603_1608Metric
- C106: value 10u -> 100n; footprint C_0805_2012Metric -> C_0603_1608Metric
- C108, C13, C67: value 100n -> 22u 50V X7R 1210; footprint C_0603_1608Metric -> C_1210_3225Metric
- C14: value 10u -> 22u 50V X7R 1210; footprint C_0805_2012Metric -> C_1210_3225Metric
- C15, C81, C82, C83, C92: value 22u 10V X7R 1210 -> 22u 50V X7R 1210
- C38: value 100n 25V -> 22u 10V X7R 1210; footprint C_0603_1608Metric -> C_1210_3225Metric
- C39: value 2.2u -> 22u 10V X7R 1210; footprint C_0603_1608Metric -> C_1210_3225Metric
- C40: value 3.3n -> 100n
- C41: value 27p -> 10u 25V 1210; footprint C_0603_1608Metric -> C_1210_3225Metric
- C42, C47, C48: value 22u 10V X7R 1210 -> 10u 25V 1210
- C44: value 100n -> 22u 10V X7R 1210; footprint C_0603_1608Metric -> C_1210_3225Metric
- C50: value 100u 10V -> 22u 10V X7R 1210; footprint C_1206_3216Metric -> C_1210_3225Metric
- C51, C55, C56: value 10u 25V 1210 -> 22u 10V X7R 1210
- C52: value 10u 25V 1210 -> 100n; footprint C_1210_3225Metric -> C_0603_1608Metric
- C53, C57: value 10u 25V 1210 -> 10n; footprint C_1210_3225Metric -> C_0603_1608Metric
- C58: value 10u 25V 1210 -> 100p; footprint C_1210_3225Metric -> C_0603_1608Metric
- C59: value 10u 25V 1210 -> 47n; footprint C_1210_3225Metric -> C_0603_1608Metric
- C60: value 10u 25V 1210 -> 4.7u; footprint C_1210_3225Metric -> C_0805_2012Metric
- C61, C62: value 10u -> 100n 25V; footprint C_0805_2012Metric -> C_0603_1608Metric
- C63, C64: value 47n -> 22u 50V X7R 1210; footprint C_0603_1608Metric -> C_1210_3225Metric
- C65: value 4.7u -> 22u 50V X7R 1210; footprint C_0805_2012Metric -> C_1210_3225Metric
- C66: value 1n -> 22u 50V X7R 1210; footprint C_0603_1608Metric -> C_1210_3225Metric
- C69: value 1u -> 100p
- C7: value 10u -> 47n; footprint C_0805_2012Metric -> C_0603_1608Metric
- C70, C88: value 22u 10V X7R 1210 -> 47n; footprint C_1210_3225Metric -> C_0603_1608Metric
- C71: value 100n 25V -> 4.7u; footprint C_0603_1608Metric -> C_0805_2012Metric
- C72: value 2.2u -> 100n 25V
- C73: value 3.3n -> 100n 25V
- C74: value 27p -> 22u 50V X7R 1210; footprint C_0603_1608Metric -> C_1210_3225Metric
- C75: value 22u 10V X7R 1210 -> 10n; footprint C_1210_3225Metric -> C_0603_1608Metric
- C76: value 22u 10V X7R 1210 -> 100p; footprint C_1210_3225Metric -> C_0603_1608Metric
- C77: value 100n -> 47n
- C78, C89: value 22u 10V X7R 1210 -> 4.7u; footprint C_1210_3225Metric -> C_0805_2012Metric
- C79, C80, C91: value 22u 10V X7R 1210 -> 100n 25V; footprint C_1210_3225Metric -> C_0603_1608Metric
- C84: value 100n 25V -> 22u 50V X7R 1210; footprint C_0603_1608Metric -> C_1210_3225Metric
- C85: value 2.2u -> 22u 50V X7R 1210; footprint C_0603_1608Metric -> C_1210_3225Metric
- C86: value 3.3n -> 10n
- C87: value 27p -> 100p
- C90: value 100n -> 100n 25V
- C94: value 22u 10V X7R 1210 -> 220n; footprint C_1210_3225Metric -> C_0603_1608Metric
- C95: value 100u 10V -> 100n; footprint C_1206_3216Metric -> C_0603_1608Metric
- C96, C97: value 100u 10V -> 330p; footprint C_1206_3216Metric -> C_0603_1608Metric
- C98: value 1u -> 10n
- C99: value 10n -> 100n
- D2: value SMBJ5.0A -> SMCJ33A (VIN_RAW clamp behind E6's filter)
- J_AB1: value A-B interconnect (IDC 2x9, top side) -> A-B interconnect (IDC 2x13, top side) to B16's underside header; footprint IDC-Header_2x09_P2.54mm_Vertical -> IDC-Header_2x13_P2.54mm_Vertical
- J_BM1: value SMP-MAX slide-on receptacle R222M00720 (underside), UHF to the dock plug -> SMP-MAX slide-on receptacle R222M00720 (underside), VHF to the dock plug
- J_BM2: value SMP-MAX slide-on receptacle R222M00720 (underside), WIFI24 to the dock plug -> SMP-MAX slide-on receptacle R222M00720 (underside), HF to the dock plug
- J_BM3: value SMP-MAX slide-on receptacle R222M00720 (underside), WIFI58 to the dock plug -> SMP-MAX slide-on receptacle R222M00720 (underside), WIFI24 to the dock plug
- J_BM4: value SMP-MAX slide-on receptacle R222M00720 (underside), SDR to the dock plug -> SMP-MAX slide-on receptacle R222M00720 (underside), GNSS to the dock plug
- J_BM5: value SMP-MAX slide-on receptacle R222M00720 (underside), LTE to the dock plug -> SMP-MAX slide-on receptacle R222M00720 (underside), SDR to the dock plug
- J_BM6: value SMP-MAX slide-on receptacle R222M00720 (underside), IRID to the dock plug -> SMP-MAX slide-on receptacle R222M00720 (underside), P2P-A to the dock plug
- J_BM7: value SMP-MAX slide-on receptacle R222M00720 (underside), LORA to the dock plug -> SMP-MAX slide-on receptacle R222M00720 (underside), P2P-B to the dock plug
- J_CN1, J_CN2, J_CN3, J_CN4: value 9 A spring pin, module return CELL_N (Mill-Max 0858 class, dock block) -> 9 A spring pin, pack return (Mill-Max 0858 class, dock block)
- J_DOCK: value spring pins to the dock block (2x6, Preci-Dip 813-S1-012-10-016101, underside): 1-4 SHORE_12V, 5-7 GND, 8 SHORE_INHIBIT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 -> spring pins to the dock block (2x6, Preci-Dip 813-S1-012-10-016101, underside): 1-4 VIN_RAW (9 to 36 V from E6), 5-7 GN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
- J_HEAT: value 12 V heating pad on the battery module (XH2.5): + - -> heater mat under the 2590 cradle (XH2.5): + -
- J_MEZZ1: value APRS mezzanine harness (IDC 2x8): I2S and I2C for the D6 codec, its gated 3.3 V, PTT lines -> D8 mezzanine harness (IDC 2x8): its USB pair, the PTT mirror, the inhibit, the PA rail state, I2C
- J_MEZZ_PWR1: value mezzanine 8 V boost feed (JST-VH): cell node through F2 (R15) -> D8 mezzanine 5 V (JST-VH): + -
- J_RF1: value SMA jack (Amphenol 132134, vertical), pigtail from the UHF module -> SMA jack (Amphenol 132134, vertical), pigtail from the VHF device
- J_RF2: value SMA jack (Amphenol 132134, vertical), pigtail from the WIFI24 module -> SMA jack (Amphenol 132134, vertical), pigtail from the HF device
- J_RF3: value SMA jack (Amphenol 132134, vertical), pigtail from the WIFI58 module -> SMA jack (Amphenol 132134, vertical), pigtail from the WIFI24 device
- J_RF4: value SMA jack (Amphenol 132134, vertical), pigtail from the SDR module -> SMA jack (Amphenol 132134, vertical), pigtail from the GNSS device
- J_RF5: value SMA jack (Amphenol 132134, vertical), pigtail from the LTE module -> SMA jack (Amphenol 132134, vertical), pigtail from the SDR device
- J_RF6: value SMA jack (Amphenol 132134, vertical), pigtail from the IRID module -> SMA jack (Amphenol 132134, vertical), pigtail from the P2P-A device
- J_RF7: value SMA jack (Amphenol 132134, vertical), pigtail from the LORA module -> SMA jack (Amphenol 132134, vertical), pigtail from the P2P-B device
- L2: value 2.2uH XAL1010-222MED (Isat 34 A, 10 mm) -> 3.3uH XAL6060-332ME (Isat 15 A); footprint L_Coilcraft_XAL1010-XXX -> L_Coilcraft_XAL6060-XXX
- L3, L4: value 2.2uH XAL1010-222MED (Isat 34 A, 10 mm) -> 4.7uH XAL6060-472ME (Isat 11 A); footprint L_Coilcraft_XAL1010-XXX -> L_Coilcraft_XAL6060-XXX
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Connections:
- net /RF_IRIDIUM renamed /RF_P2PA
- net /RF_LORA renamed /RF_P2PB
- net /RF_UHF renamed /RF_VHF
- C100 pad 1: /HEAT_IN -> /U22_DVDT
- C101 pad 1: +3V3 -> /VBAT
- C104 pad 1: /+5V_M1 -> +3V3
- C106 pad 1: /5V_WALL -> +3V3
- C108 pad 1: +3V3 -> /VBAT
- C13 pad 1: /BST33 -> /VBUS20
- C13 pad 2: /SW33 -> GND
- C14 pad 1: /+5V_M1 -> /VBUS20
- C15 pad 1: +3V3 -> /VBUS20
- C38 pad 1: /BST1 -> /+5V_S2
- C38 pad 2: /SW1 -> GND
- C39 pad 1: /VCC1 -> /+5V_S2
- C40 pad 1: /COMP1C -> /S3_BOOT
- C40 pad 2: GND -> /S3_SW
- C41 pad 1: /COMP1 -> /VBAT
- C42 pad 1: /BOOST1_IN -> /VBAT
- C43 pad 1: /BOOST1_IN -> /+5V_S3
- C44 pad 1: /BOOST1_IN -> /+5V_S3
- C45 pad 1: /+5V_M1 -> /+5V_S3
- C46 pad 1: /+5V_M1 -> /SD_BOOT
- C46 pad 2: GND -> /SD_SW
- C47 pad 1: /+5V_M1 -> /VBAT
- C48 pad 1: /+5V_M1 -> /VBAT
- C49 pad 1: /+5V_M1 -> /+5V_DEV
- C50 pad 1: /CELL+ -> /+5V_DEV
- C51 pad 1: /SHORE_12V -> /+5V_DEV
- C52 pad 1: /SHORE_12V -> /B33_BST
- C52 pad 2: GND -> /B33_SW
- C53 pad 1: /PMID -> /B33_SS
- C54 pad 1: /PMID -> /VBAT
- C55 pad 1: /PMID -> +3V3
- C56 pad 1: /SYS_CHG -> +3V3
- C57 pad 1: /SYS_CHG -> /PA_COMPC
- C58 pad 1: /SYS_CHG -> /PA_COMP
- C59 pad 1: /SYS_CHG -> /PA_SS
- C60 pad 1: /SYS_CHG -> /PA_VCC
- C61 pad 1: /CELL+ -> /PA_BOOT1
- C61 pad 2: GND -> /PA_SW1
- C62 pad 1: /CELL+ -> /PA_BOOT2
- C62 pad 2: GND -> /PA_SW2
- C63 pad 1: /BTST1 -> /VBAT
- C63 pad 2: /SW1_CHG -> GND
- C64 pad 1: /BTST2 -> /VBAT
- C64 pad 2: /SW2_CHG -> GND
- C65 pad 1: /REGN -> /+13V8_PA
- C66 pad 1: /SDRV -> /+13V8_PA
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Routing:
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- added copper zone on In2.Cu, net /VBAT
- added copper zone on In4.Cu, net GND
- removed copper zone on F.Cu, net /+5V_M1
- removed copper zone on In2.Cu, net /+5V_M1
- removed copper zone on B.Cu, net /+5V_M2
- removed copper zone on F.Cu, net /+5V_M2
- removed copper zone on B.Cu, net /+5V_PI
- removed copper zone on F.Cu, net /+5V_PI
- removed copper zone on B.Cu, net /BOOST1_IN
- removed copper zone on F.Cu, net /BOOST1_IN
- removed copper zone on In1.Cu, net /BOOST1_IN
- removed copper zone on In2.Cu, net /BOOST1_IN
- removed copper zone on B.Cu, net /BOOST2_IN
- removed copper zone on F.Cu, net /BOOST2_IN
- removed copper zone on In1.Cu, net /BOOST2_IN
- removed copper zone on In2.Cu, net /BOOST2_IN
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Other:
- board size 285 x 160 mm -> 240 x 160 mm
- copper layers 4 -> 6
- board text added: "3.3 V BUCK, CONTROL PASSIVES"
- board text added: "BB-2590/U PACK IN ITS CRADLE WEST OF THIS BOARD (32.49 item 12), ITS CABLE INTO E6, THE NODE OVER THE DOCK PINS"
- board text added: "BM 5G DIV"
- board text added: "BM 5G MAIN"
- board text added: "BM HF"
- board text added: "BM P2P A"
- board text added: "BM P2P B"
- board text added: "BM VHF"
- board text added: "CHARGER BQ25731 4S FROM THE 20 V BUS"
- board text added: "CONTROL: LTC2954, EXPANDERS, EMCON GATES"
- board text added: "D8 MEZZANINE SITE 100 x 80"
- board text added: "DOCK BLOCK (underside): J_DOCK 2x6 + 9 A pins + pre-charge pin, land on E6's block"
- board text added: "F1 25 A"
- board text added: "FRONT END: LM5176 9-36 V -> 20 V BUS"
- board text added: "HF RAIL: TPS55288 12 V"
- board text added: "J_AB1 2x13 -> B16 underside (113, -46)"
- board text added: "J_MEZZ_PWR1 VH2 (5 V)"
- board text added: "LEAD CONNECTORS"
- board text added: "MESHSAT FIELD KIT - PCB-A POWER + I/O - REV A (A18)"
- board text added: "MESHSAT-830 | 240 x 160 x 1.6 mm FR-4, 6 layers JLC06161H-3313 | matte black | 2026-09-07"
- board text added: "PA RAIL: LM5176 13.8 V (PA ON THE PLATE)"
- board text added: "PCB-A UNDERSIDE - 13.4 mm above the dock strip E6; the dock block pins and eleven SMP-MAX receptacles land on the dock"
- board text added: "POE RAIL: LM5176 BOOST 54 V"
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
